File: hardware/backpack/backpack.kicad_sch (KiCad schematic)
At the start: 22 parts, among them J2 Conn_02x06_Top_Bottom, J3 Conn_02x06_Top_Bottom, J7 USB_C, J8 MICROMOD-2222, J9 USB_C

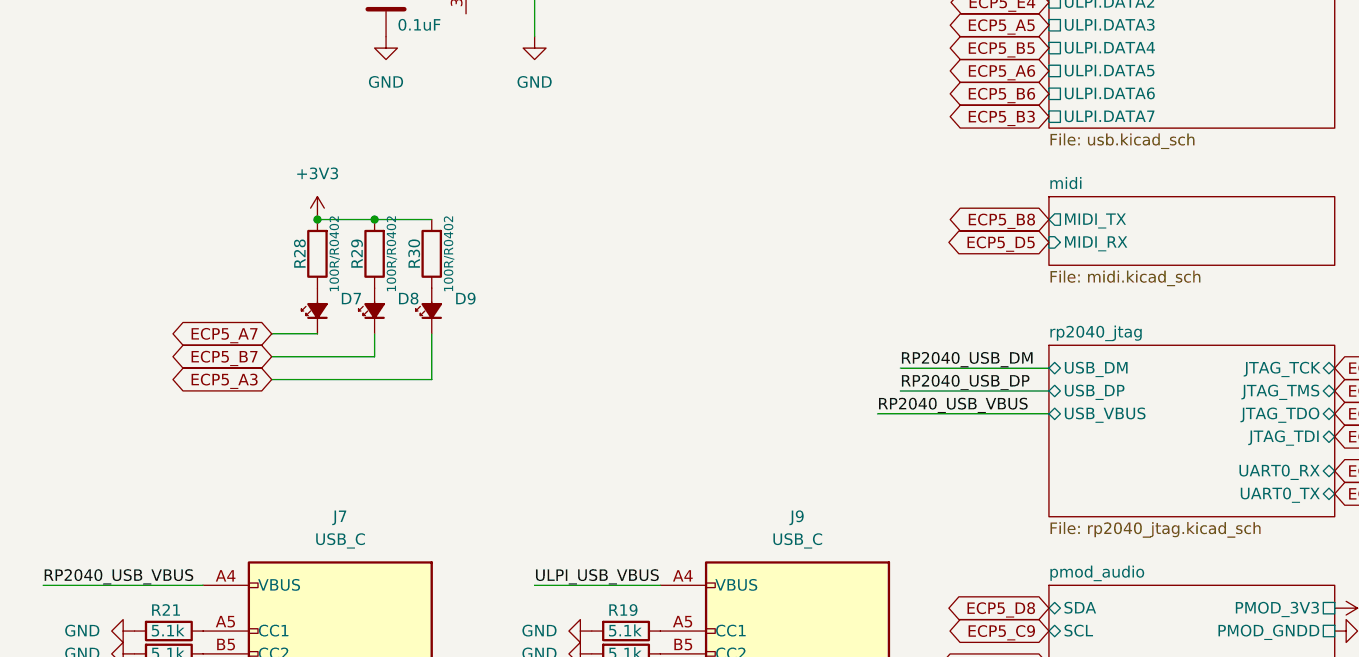
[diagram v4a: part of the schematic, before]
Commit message: place 2 leds, route 2nd button to both FPGA and RP2040
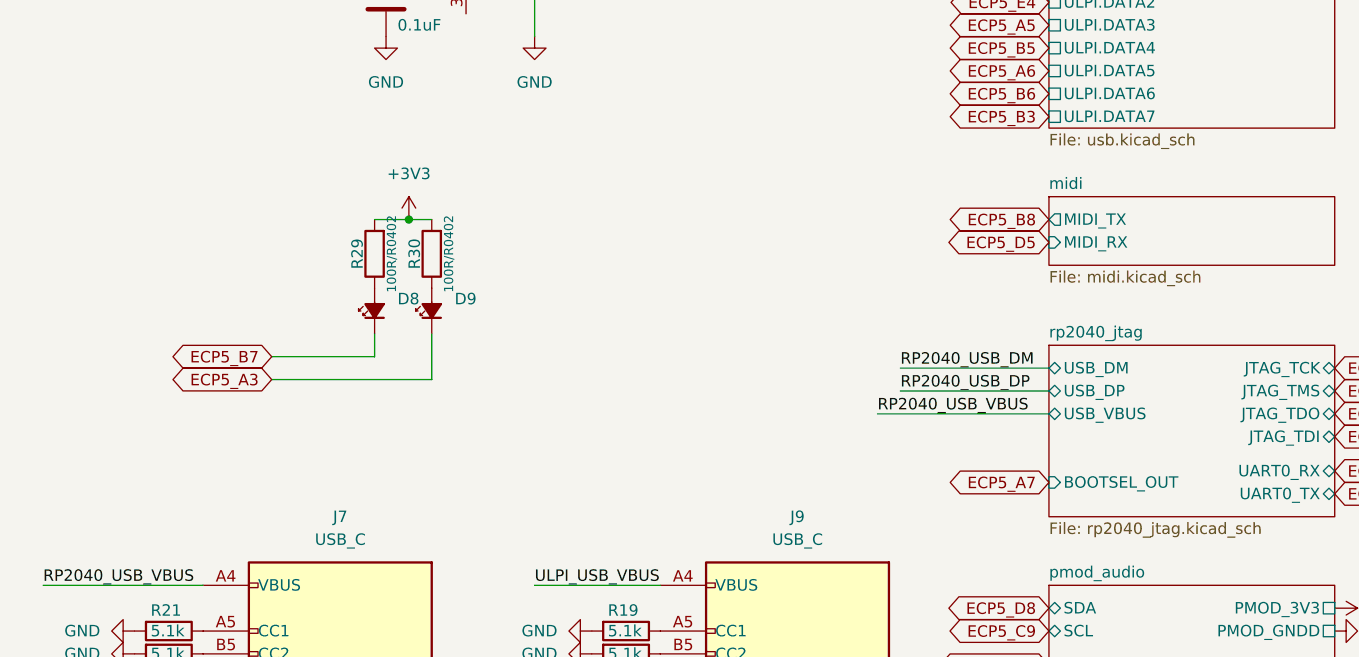
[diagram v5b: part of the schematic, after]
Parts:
- removed D7: LED 0402 RED, LED_SMD:LED_0402_1005Metric, symbol Device:LED_Small_Filled
- removed R28: 100R/R0402, Resistor_SMD:R_0402_1005Metric, symbol OLIMEX_RCL:R
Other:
- sheet rp2040_jtag ports: added BOOTSEL_OUT; removed none
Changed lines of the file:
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@@
 	)
 	(junction
-		(at 194.31 134.62)
+		(at 167.64 78.74)
 		(diameter 0)
 		(color 0 0 0 0)
 	)
 	(junction
-		(at 157.48 78.74)
+		(at 194.31 134.62)
 		(diameter 0)
 		(color 0 0 0 0)
@@
 		(color 0 0 0 0)
 	)
-	(junction
-		(at 163.83 78.74)
-		(diameter 0)
-		(color 0 0 0 0)
-	)
 	(no_connect
 		(at 21.59 97.79)
@@
 	(wire
 		(pts
-			(xy 157.48 78.74) (xy 163.83 78.74)
+			(xy 167.64 78.74) (xy 163.83 78.74)
 		)
 		(stroke
@@
 	(wire
 		(pts
-			(xy 152.4 91.44) (xy 157.48 91.44)
+			(xy 165.1 45.72) (xy 165.1 50.8)
 		)
 		(stroke
@@
 	(wire
 		(pts
-			(xy 165.1 45.72) (xy 165.1 50.8)
+			(xy 194.31 134.62) (xy 195.58 134.62)
 		)
 		(stroke
@@
 	(wire
 		(pts
-			(xy 194.31 134.62) (xy 195.58 134.62)
+			(xy 167.64 78.74) (xy 170.18 78.74)
 		)
 		(stroke
@@
 	(wire
 		(pts
-			(xy 163.83 78.74) (xy 170.18 78.74)
-		)
-		(stroke
-			(width 0)
-			(type default)
-		)
-	)
-	(wire
-		(pts
 			(xy 194.31 132.08) (xy 194.31 134.62)
 		)
@@
 	(global_label "ECP5_A7"
 		(shape bidirectional)
-		(at 152.4 91.44 180)
+		(at 238.76 107.95 180)
 		(fields_autoplaced yes)
 		(effects
@@
 		)
 		(property "Intersheetrefs" "${INTERSHEET_REFS}"
-			(at 140.9523 91.44 0)
+			(at 227.3123 107.95 0)
 			(effects
 				(font
@@
 	)
 	(symbol
-		(lib_id "Device:LED_Small_Filled")
-		(at 157.48 88.9 90)
-		(unit 1)
-		(exclude_from_sim no)
-		(in_bom yes)
-		(on_board yes)
-		(dnp no)
-		(fields_autoplaced yes)
-		(property "Reference" "D7"
-			(at 160.02 87.5664 90)
-			(effects
-				(font
-					(size 1.27 1.27)
-				)
-				(justify right)
-			)
-		)
-		(property "Value" "LED 0402 RED"
-			(at 160.02 90.1064 90)
-			(effects
-				(font
-					(size 1.27 1.27)
-				)
-				(justify right)
-				(hide yes)
-			)
-		)
-		(property "Footprint" "LED_SMD:LED_0402_1005Metric"
-			(at 157.48 88.9 90)
-			(effects
-				(font
-					(size 1.27 1.27)
-				)
-				(hide yes)
-			)
-		)
-		(property "Datasheet" "~"
-			(at 157.48 88.9 90)
-			(effects
-				(font
-					(size 1.27 1.27)
-				)
-				(hide yes)
-			)
-		)
-		(property "Description" "Light emitting diode, small symbol, filled shape"
-			(at 157.48 88.9 0)
-			(effects
-				(font
-					(size 1.27 1.27)
-				)
-				(hide yes)
-			)
-		)
-		(property "lcsc#" "C965790"
-			(at 157.48 88.9 90)
-			(effects
-				(font
-					(size 1.27 1.27)
-				)
-				(hide yes)
-			)
-		)
-		(pin "2"
-		)
-		(pin "1"
-		)
-		(instances
-			(project "backpack"
-				(path "/df6062c3-a570-4505-924c-c7fe32df3670"
-					(reference "D7")
-					(unit 1)
-				)
-			)
-		)
-	)
-	(symbol
-		(lib_id "OLIMEX_RCL:R")
-		(at 157.48 82.55 90)
-		(unit 1)
-		(exclude_from_sim yes)
-		(in_bom yes)
-		(on_board yes)
-		(dnp no)
-		(property "Reference" "R28"
-			(at 155.575 82.55 0)
-			(effects
-				(font
-					(size 1.27 1.27)
-				)
-			)
-		)
-		(property "Value" "100R/R0402"
-			(at 159.385 82.55 0)
-			(effects
-				(font
-					(size 1.016 1.016)
-				)
-			)
-		)
-		(property "Footprint" "Resistor_SMD:R_0402_1005Metric"
-			(at 159.258 82.55 0)
-			(effects
-				(font
-					(size 0.762 0.762)
-				)
-				(hide yes)
-			)
-		)
-		(property "Datasheet" ""
-			(at 157.48 82.55 90)
-			(effects
-				(font
-					(size 0.762 0.762)
-				)
-			)
-		)
-		(property "Description" ""
-			(at 157.48 82.55 0)
-			(effects
-				(font
-					(size 1.27 1.27)
-				)
-				(hide yes)
-			)
-		)
-		(property "lcsc#" "  C106232"
-			(at 157.48 82.55 0)
-			(effects
-				(font
-					(size 1.27 1.27)
-				)
-				(hide yes)
-			)
-		)
-		(pin "1"
-		)
-		(pin "2"
-		)
-		(instances
-			(project "backpack"
-				(path "/df6062c3-a570-4505-924c-c7fe32df3670"
-					(reference "R28")
-					(unit 1)
-				)
-			)
-		)
-	)
-	(symbol
 		(lib_id "Connector:USB_C_Receptacle_USB2.0")
 		(at 160.02 134.62 0)
@@
 	(symbol
 		(lib_id "power:+3V3")
-		(at 157.48 78.74 0)
+		(at 167.64 78.74 0)
 		(unit 1)
 		(exclude_from_sim no)
@@
 		(fields_autoplaced yes)
 		(property "Reference" "#PWR041"
-			(at 157.48 82.55 0)
+			(at 167.64 82.55 0)
 			(effects
 				(font
@@
 		)
 		(property "Value" "+3V3"
-			(at 157.48 73.66 0)
+			(at 167.64 73.66 0)
 			(effects
 				(font
@@
 		)
 		(property "Footprint" ""
-			(at 157.48 78.74 0)
+			(at 167.64 78.74 0)
 			(effects
 				(font
@@
 		)
 		(property "Datasheet" ""
-			(at 157.48 78.74 0)
+			(at 167.64 78.74 0)
 			(effects
 				(font
@@
 		)
 		(property "Description" ""
-			(at 157.48 78.74 0)
+			(at 167.64 78.74 0)
 			(effects
 				(font
@@
 			(effects
 				(font
+					(size 1.27 1.27)
+				)
+				(justify left)
+			)
+		)
+		(pin "BOOTSEL_OUT" input
+			(at 238.76 107.95 180)
+			(effects
+				(font

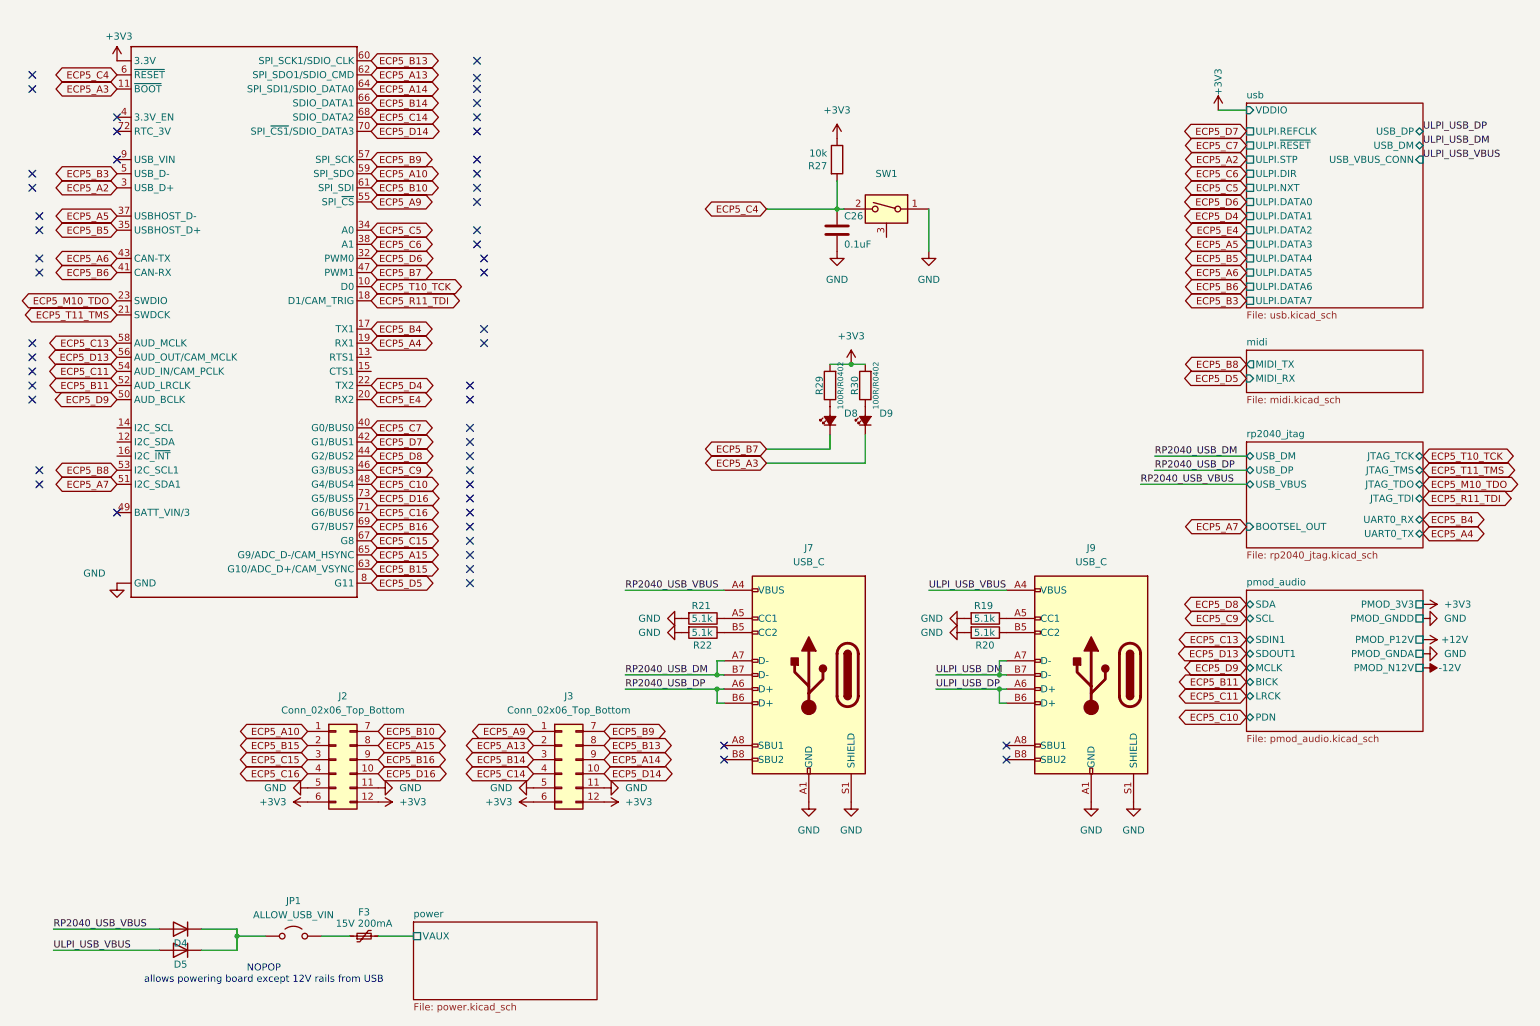
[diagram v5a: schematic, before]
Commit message: fix footprint errors and pin assignments on ffc
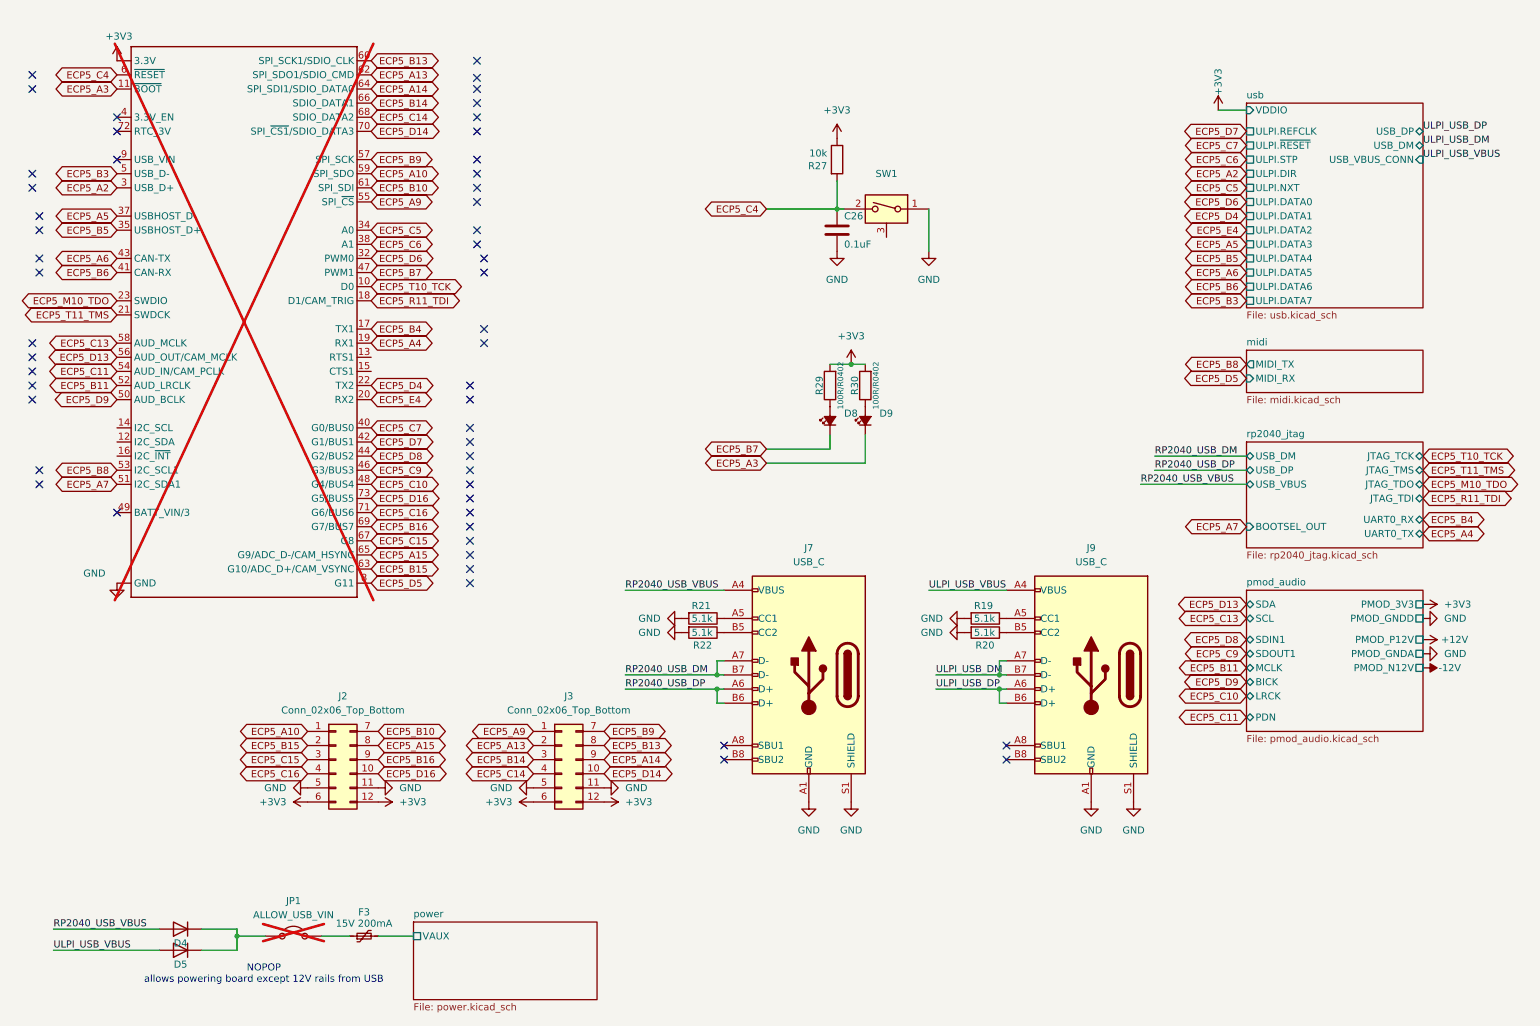
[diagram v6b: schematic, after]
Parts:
- J2, J3: lcsc# (none) -> C2897426
- J7, J9: lcsc# (none) -> C165948
- J8, JP1: now not fitted
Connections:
- net GND: now also J8.S1 (GND), J8.S2 (GND); no longer J8.GND1 (GND), J8.GND2 (GND), J8.GND3 (GND)
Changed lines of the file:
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@@
 	(global_label "ECP5_C11"
 		(shape bidirectional)
-		(at 238.76 138.43 180)
+		(at 238.76 142.24 180)
 		(fields_autoplaced yes)
 		(effects
@@
 		)
 		(property "Intersheetrefs" "${INTERSHEET_REFS}"
-			(at 225.9214 138.43 0)
+			(at 225.9214 142.24 0)
 			(effects
 				(font
@@
 	(global_label "ECP5_C13"
 		(shape bidirectional)
-		(at 238.76 128.27 180)
+		(at 238.76 124.46 180)
 		(fields_autoplaced yes)
 		(effects
@@
 		)
 		(property "Intersheetrefs" "${INTERSHEET_REFS}"
-			(at 225.9214 128.27 0)
+			(at 225.9214 124.46 0)
 			(effects
 				(font
@@
 	(global_label "ECP5_A2"
 		(shape bidirectional)
-		(at 238.76 41.91 180)
+		(at 238.76 44.45 180)
 		(fields_autoplaced yes)
 		(effects
@@
 		)
 		(property "Intersheetrefs" "${INTERSHEET_REFS}"
-			(at 227.3123 41.91 0)
+			(at 227.3123 44.45 0)
 			(effects
 				(font
@@
 	(global_label "ECP5_C9"
 		(shape bidirectional)
-		(at 238.76 124.46 180)
+		(at 238.76 130.81 180)
 		(fields_autoplaced yes)
 		(effects
@@
 		)
 		(property "Intersheetrefs" "${INTERSHEET_REFS}"
-			(at 226.3179 124.46 0)
+			(at 226.3179 130.81 0)
 			(effects
 				(font
@@
 	(global_label "ECP5_C6"
 		(shape bidirectional)
-		(at 238.76 44.45 180)
+		(at 238.76 41.91 180)
 		(fields_autoplaced yes)
 		(effects
@@
 		)
 		(property "Intersheetrefs" "${INTERSHEET_REFS}"
-			(at 226.3179 44.45 0)
+			(at 226.3179 41.91 0)
 			(effects
 				(font
@@
 	(global_label "ECP5_C10"
 		(shape bidirectional)
-		(at 238.76 142.24 180)
+		(at 238.76 138.43 180)
 		(fields_autoplaced yes)
 		(effects
@@
 		)
 		(property "Intersheetrefs" "${INTERSHEET_REFS}"
-			(at 225.1084 142.24 0)
+			(at 225.1084 138.43 0)
 			(effects
 				(font
@@
 	(global_label "ECP5_D8"
 		(shape bidirectional)
-		(at 238.76 121.92 180)
+		(at 238.76 128.27 180)
 		(fields_autoplaced yes)
 		(effects
@@
 		)
 		(property "Intersheetrefs" "${INTERSHEET_REFS}"
-			(at 226.3179 121.92 0)
+			(at 226.3179 128.27 0)
 			(effects
 				(font
@@
 	(global_label "ECP5_D9"
 		(shape bidirectional)
-		(at 238.76 133.35 180)
+		(at 238.76 135.89 180)
 		(fields_autoplaced yes)
 		(effects
@@
 		)
 		(property "Intersheetrefs" "${INTERSHEET_REFS}"
-			(at 227.1309 133.35 0)
+			(at 227.1309 135.89 0)
 			(effects
 				(font
@@
 	(global_label "ECP5_D13"
 		(shape bidirectional)
-		(at 238.76 130.81 180)
+		(at 238.76 121.92 180)
 		(fields_autoplaced yes)
 		(effects
@@
 		)
 		(property "Intersheetrefs" "${INTERSHEET_REFS}"
-			(at 225.9214 130.81 0)
+			(at 225.9214 121.92 0)
 			(effects
 				(font
@@
 	(global_label "ECP5_B11"
 		(shape bidirectional)
-		(at 238.76 135.89 180)
+		(at 238.76 133.35 180)
 		(fields_autoplaced yes)
 		(effects
@@
 		)
 		(property "Intersheetrefs" "${INTERSHEET_REFS}"
-			(at 225.9214 135.89 0)
+			(at 225.9214 133.35 0)
 			(effects
 				(font
@@
 		(in_bom yes)
 		(on_board yes)
-		(dnp no)
+		(dnp yes)
 		(property "Reference" "J8"
 			(at 38.1 21.082 0)
@@
 		(pin "9"
 		)
-		(pin "GND1"
-		)
-		(pin "GND2"
+		(pin "S1"
 		)
-		(pin "GND3"
+		(pin "S2"
 		)
 		(instances
@@
 		(in_bom yes)
 		(on_board yes)
-		(dnp no)
+		(dnp yes)
 		(fields_autoplaced yes)
 		(property "Reference" "JP1"
@@
 			)
 		)
+		(property "lcsc#" "C165948"
+			(at 160.02 134.62 0)
+			(effects
+				(font
+					(size 1.27 1.27)
+				)
+				(hide yes)
+			)
+		)
 		(pin "A1"
 		)
@@
 			)
 		)
+		(property "lcsc#" "C2897426"
+			(at 74.93 149.86 0)
+			(effects
+				(font
+					(size 1.27 1.27)
+				)
+				(hide yes)
+			)
+		)
 		(pin "5"
 		)
@@
 			)
 		)
+		(property "lcsc#" "C165948"
+			(at 210.82 134.62 0)
+			(effects
+				(font
+					(size 1.27 1.27)
+				)
+				(hide yes)
+			)
+		)
 		(pin "A1"
 		)
@@
 			(at 115.57 149.86 0)
 			(effects
+				(font
+					(size 1.27 1.27)
+				)
+				(hide yes)
+			)
+		)
+		(property "lcsc#" "C2897426"
+			(at 115.57 149.86 0)
+			(effects
